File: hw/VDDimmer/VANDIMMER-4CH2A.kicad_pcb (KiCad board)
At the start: 2 copper layers, 100 x 80 mm, 96 parts, among them J1 USB-C 16P, J10 A2 V+SEL VIN/5V, J11 BTN1, J12 BTN2, J13 EXP 3V3/GND/SDA/SCL/EN/IO0, J14 UART1 3V3/GND/TX/RX, J2 VIN 9-24V, J3 CH1 V+/LED-, J4 CH2 V+/LED-, J5 CH3 V+/LED-, J6 CH4 V+/LED-, J7 ADDR1 V+/D/CLK/GND, J8 ADDR2 V+/D/CLK/GND, J9 A1 V+SEL VIN/5V, Q1 20N06, Q2 20N06, Q3 20N06, Q4 20N06, Q5 SUD50P06-15, U1 ESP32-S3-WROOM-1U-N16, U2 AP63301WU-7, U3 AMS1117-3.3, U4 74HCT125, U5 74HCT125

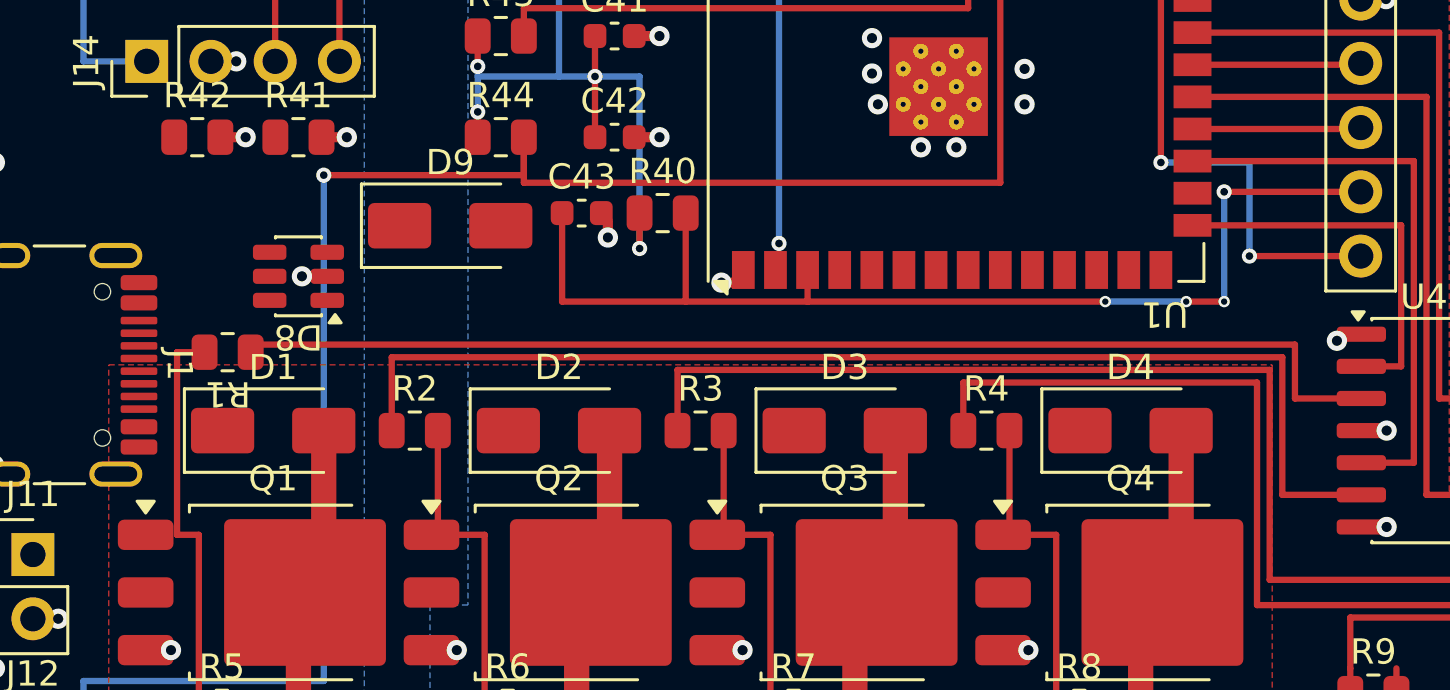
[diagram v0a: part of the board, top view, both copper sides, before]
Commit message: Re-route USB into the flipped J1; move R1 clear of the fan-out
R1 was straddling y 110.550..112.450, which after the flip is exactly where
J1's four D+/D- pads sit (111.1..112.9). With J1's pads ending at x 108.420 and
R1's courtyard starting at 109.520, the escape corridor was 1.10 mm - two lanes
for six signals.

R1 moved 2.3 mm east to (113.5, 111.5), into the 2.65 mm gap between D8's
courtyard (ends y 110.200) and D1's (starts y 112.850). Its GDRV1 pad lands at
x 113.9..114.925, still directly on GDRV1's existing y=111.2 lane, so that
connection cost nothing; only the now-stubbed western segment was trimmed.
Corridor goes 1.10 -> 3.40 mm.

GATE1 re-routed out of R1's west pad and down the back of J1 on B.Cu
(x 112.5, y 112.9..117.5, then west to 108.5) to Q1's gate, keeping it out of
the USB region entirely.

Fan-out assigned by planar ordering - source y ascending maps to turn-x
ascending, so no horizontal crosses the vertical of a pad further north:
  CC1 A5  y110.75 -> lane 108.75 -> R41.1
  DM  B7  y111.25 -> lane 109.20 -> D8.4
  DP  A6  y111.75 -> lane 109.65 -> D8.6
  DM  A7  y112.25 -> B.Cu at x110.35 (the one forced crossing)
  DP  B6  y112.75 -> lane 111.05, joins DP's run
CC2 and VBUS are boxed in by D1, so both take B.Cu: CC2 at x 108.96 down to
R42.1, VBUS south of D1 then north at x 111.2 to D8.5.

One error caught by DRC that my offline checker missed: the DM via at
(110.35, 112.25) sat 0.075 mm from DP's y=112.75 run. route.py does not
synthesise vias at layer transitions, so it only checked the tracks. Via moved
to (110.35, 112.0) and the check script now sweeps proposed vias against every
pad, track and via explicitly.

Co-Authored-By: Claude Opus 5 (1M context) <noreply@anthropic.com>
Claude-Session: https://claude.ai/code/session_01XeXr1isxVCg8kRo5Eh8BHM
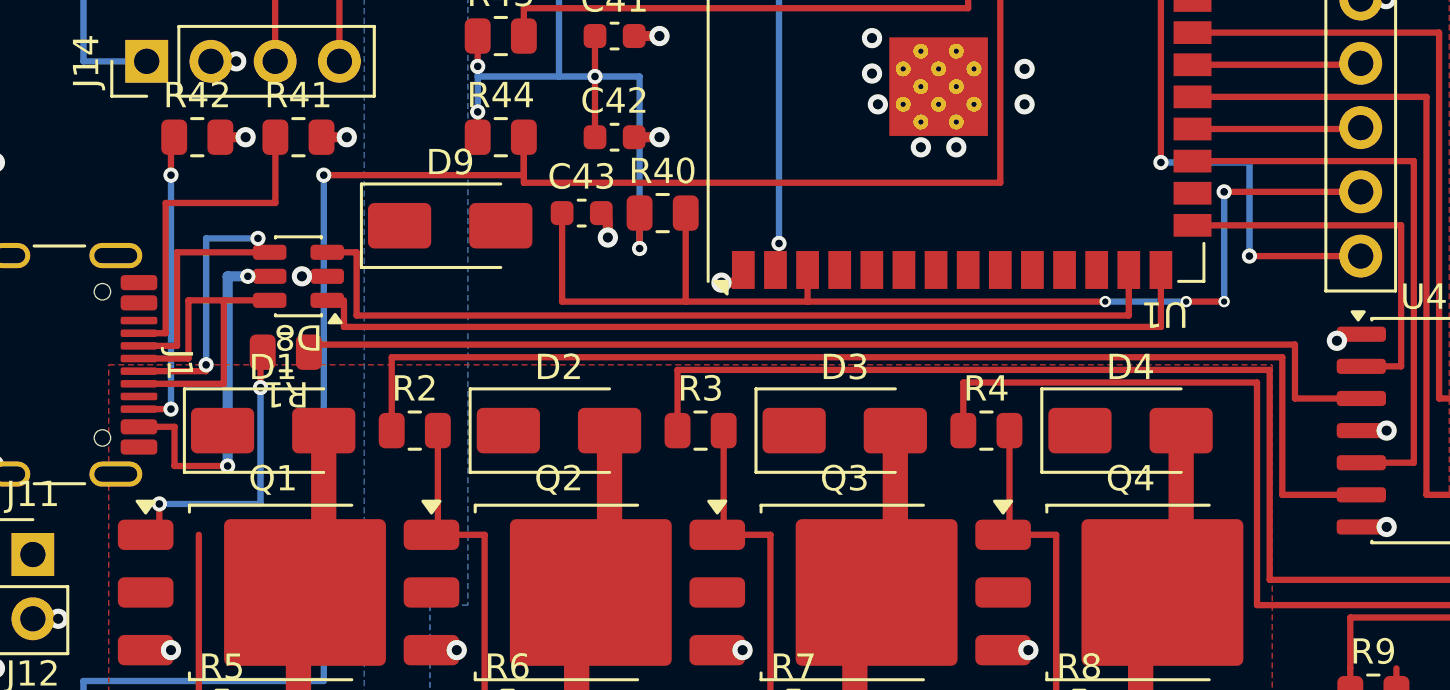
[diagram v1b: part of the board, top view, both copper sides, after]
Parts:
- moved R1 2.30 mm to (113.5, 111.5)
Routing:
- net /MCU/USB_DM: track 0.00 -> 51.7 mm, vias 0 -> 2
- net /MCU/USB_DP: track 0.00 -> 46.9 mm
- net /MCU/VBUS: track 0.00 -> 12.6 mm, vias 0 -> 2
- net /MCU/USB_CC1: track 0.00 -> 11.7 mm
- net /MCU/USB_CC2: track 0.00 -> 10.6 mm, vias 0 -> 2
- net /PWM/GDRV1: track 46.0 -> 43.8 mm
- net /PWM/GATE1: track 16.0 -> 17.4 mm, vias 0 -> 2

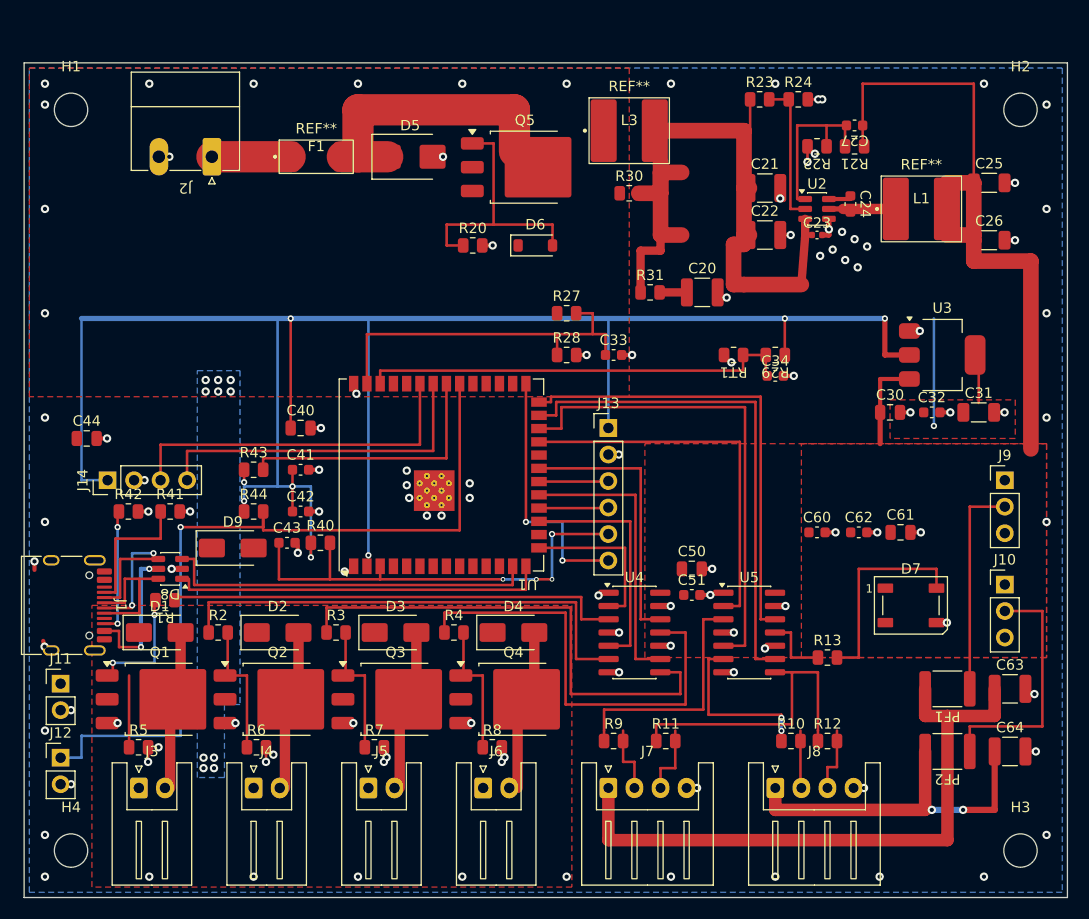
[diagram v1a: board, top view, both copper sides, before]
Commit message: Relink GATE1, brace D1's anode, re-drill sub-IPC vias, add GND return vias
- GATE1 lost the Q1-gate-to-pulldown link when the descent was re-routed; the
  1.20 mm and 6.88 mm fragments are rejoined at y=118.72.
- D1's anode was down to a single thermal spoke from the VIN_PROT pour after
  R1 moved. A 0.5 mm stub north into the pour body gives it solid copper.
- The 4 remaining 0.45/0.25 vias (all EN_MCU) gave a 0.100 mm annular ring,
  under IPC Class 2's 0.125 mm. Re-drilled to 0.45/0.20 = 0.125 exactly, which
  also still satisfies the board's own min_via_drill of 0.2. The other six of
  the original ten went out with the USB rework.
- 33 GND return vias placed, one beside each layer transition that had no
  ground via within 1.0 mm - the EMC finding kicad-happy raised and I confirmed
  (39 of 39 transitions were bare, nearest 2.47 mm, worst 8.43 mm). All 33
  positions were clearance-checked against every pad, track and via first.
  Six transitions have no room and are left bare: EN_MCU x3, VBUS x2,
  USB_DM x1.

Co-Authored-By: Claude Opus 5 (1M context) <noreply@anthropic.com>
Claude-Session: https://claude.ai/code/session_01XeXr1isxVCg8kRo5Eh8BHM
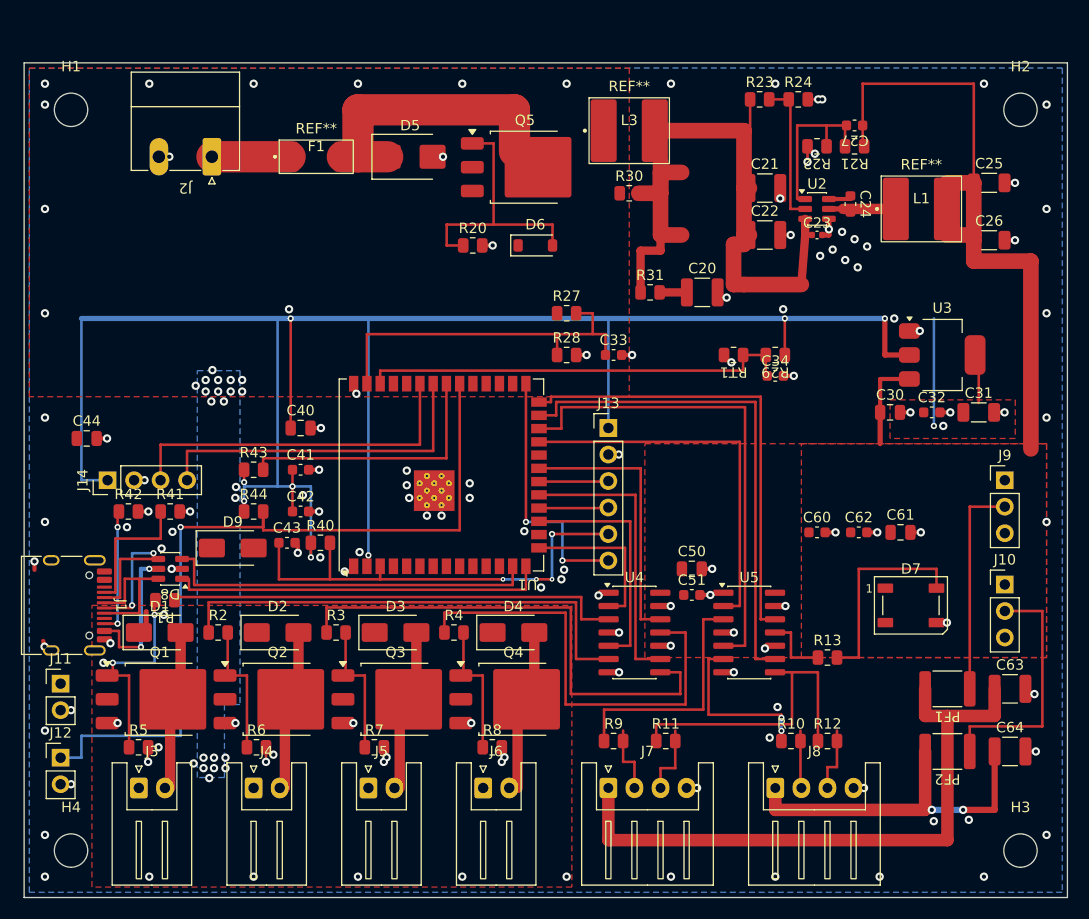
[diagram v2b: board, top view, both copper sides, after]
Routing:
- net /PWM/GATE1: track 17.4 -> 18.9 mm
- net VIN_PROT: track 0.00 -> 1.10 mm, vias 10 -> 14
- net GND: vias 116 -> 145

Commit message: Fix four dead-on-arrival defects hiding behind a clean DRC
DRC reports a split net as an unconnected item, never an error, so the board
read "0 errors" while both the gate drivers and the MCU were unpowered. All
20 unconnected items had been written off as benign; four were not.

- U4's gate drivers had no +5V. The F.Cu pour filled as two islands that did
  not touch, 448.6 mm2 carrying the main rail and 123.1 mm2 carrying only
  U4.14/C50.1/C51.1. The four-wire addressable bus runs the full height of the
  zone at 0.5 mm pitch and nothing can fill between the traces. Bridged on B.Cu
  across the bus only: +5V vias at (167.6,105.0) and (171.6,105.0), 4.0 mm of
  0.5 mm track, both vias landing inside their own island's fill.
- U1, the ESP32, had no 3V3. The via at (133.0,107.2) was exactly tangent to
  pad U1.2 -- centre-to-pad-box 0.3000 mm against a via radius of 0.3000 mm,
  zero overlap. Added a 0.5 mm F.Cu stub 0.75 mm into the pad.
- J1's north GND pad was floating; USB return had only the shell. Joined to the
  adjacent shield pad.
- Deleted a 10.3 mm orphan +3V3 B.Cu stub dangling at both ends.

Added an F.Cu GND pour at priority 0, with a bite out of the top edge at
x 172.5-186.0, y 60.5-78.5 to keep ground copper off SW and the FB divider.
75 GND vias previously touched no F.Cu copper at all, so the return vias added
in 1a1d10b were inert. via_dangling 81 -> 9, GND groups 2 -> 1, warnings
244 -> 170, unconnected 18 -> 15. Zone set to solid pad connection to clear
six starved_thermal errors.

Tooling: measure.py did not run as committed (missing import, two wrong call
signatures, a zone parser matching spaces against a tab-indented file). New
connect.py groups each net's copper into connected components and is what found
all four defects; its first version treated a touching via and pad as connected,
which is precisely the U1.2 case, so it now requires real overlap and reports
contacts thinner than 50 um. Also polyidx.py, emc.py, retvia.py.

Co-Authored-By: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
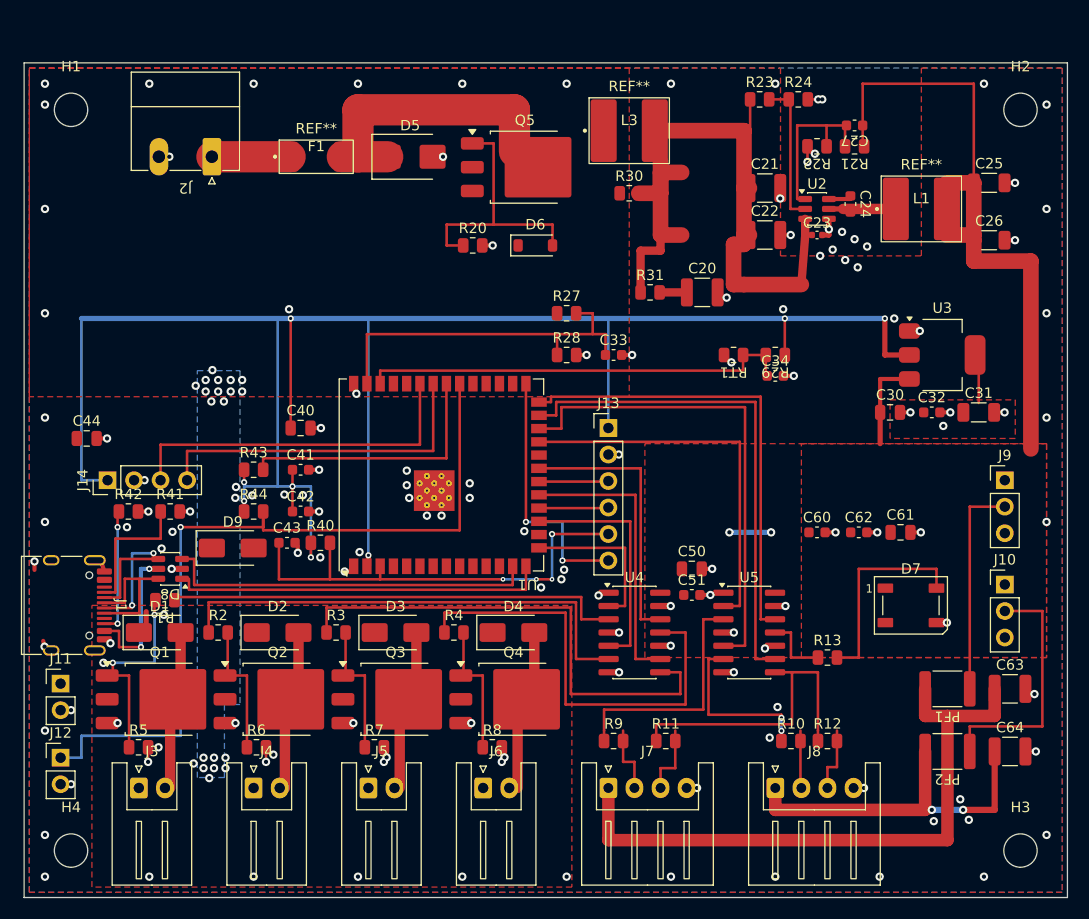
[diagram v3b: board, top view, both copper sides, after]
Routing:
- net +3V3: track 195.5 -> 186.3 mm, vias 9 -> 8
- net +5V: track 69.1 -> 73.1 mm, vias 0 -> 2
- net GND: track 27.3 -> 28.4 mm, vias 145 -> 148
- added copper zone on F.Cu, net GND
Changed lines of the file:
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@@
 		(net "+5V")
 	)
+	(via
+		(at 167.6 105)
+		(size 0.8)
+		(drill 0.4)
+		(layers "F.Cu" "B.Cu")
+		(net "+5V")
+	)
+	(via
+		(at 171.6 105)
+		(size 0.8)
+		(drill 0.4)
+		(layers "F.Cu" "B.Cu")
+		(net "+5V")
+	)
+	(segment
+		(start 167.6 105)
+		(end 171.6 105)
+		(width 0.5)
+		(layer "B.Cu")
+		(net "+5V")
+	)
 	(segment
 		(start 123.186 125.6)
@@
 	)
 	(segment
+		(start 107.695 108.75)
+		(end 107.35 107.68)
+		(width 0.4)
+		(layer "F.Cu")
+		(net "GND")
+	)
+	(segment
 		(start 175.113 63.5)
 		(end 176.5 63.5)
@@
 	)
 	(via
+		(at 189.728 130.586)
+		(size 0.8)
+		(drill 0.4)
+		(layers "F.Cu" "B.Cu")
+		(net "GND")
+	)
+	(via
 		(at 125.394 83.614)
 		(size 0.8)
@@
 	)
 	(via
+		(at 124.947 101.378)
+		(size 0.8)
+		(drill 0.4)
+		(layers "F.Cu" "B.Cu")
+		(net "GND")
+	)
+	(via
 		(at 116.447 90.95)
 		(size 0.8)
@@
 	)
 	(via
+		(at 121.866 101.455)
+		(size 0.8)
+		(drill 0.4)
+		(layers "F.Cu" "B.Cu")
+		(net "GND")
+	)
+	(via
 		(at 165.775 111)
 		(size 0.8)
@@
 	)
 	(segment
+		(start 133 107.2)
+		(end 133 108.25)
+		(width 0.5)
+		(layer "F.Cu")
+		(net "+3V3")
+	)
+	(segment
 		(start 127.488 107.4)
 		(end 127.488 106.4)
@@
 	)
 	(via
-		(at 187.2 94.8)
-		(size 0.6)
-		(drill 0.3)
-		(layers "F.Cu" "B.Cu")
-		(net "+3V3")
-	)
-	(via
 		(at 182.5 84.5)
 		(size 0.6)
@@
 	)
 	(segment
-		(start 187.2 84.5)
-		(end 187.2 94.8)
-		(width 0.25)
-		(layer "B.Cu")
-		(net "+3V3")
-	)
-	(segment
 		(start 124.3 100.6)
 		(end 127.488 100.6)
@@
 			)
 		)
+	)
+	(zone
+		(net "GND")
+		(layer "F.Cu")
+		(hatch edge 0.508)
+		(connect_pads yes
+			(clearance 0.2)
+		)
+		(min_thickness 0.25)
+		(fill yes
+			(thermal_gap 0.5)
+			(thermal_bridge_width 0.5)
+			(island_removal_mode 0)
+		)
+		(polygon
+			(pts
+				(xy 100.5 60.5) (xy 172.5 60.5) (xy 172.5 78.5) (xy 186 78.5) (xy 186 60.5) (xy 199.5 60.5) (xy 199.5 139.5)
+				(xy 100.5 139.5)
+			)
+		)

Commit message: Fix six drill defects, fit the I2C pull-ups, add the board ID
Drill defects
-------------
hole_to_hole and holes_co_located are downgraded to warning in .kicad_pro, so
the board reported "DRC 0 errors" while carrying five hole_to_hole and one
holes_co_located -- two of them with physically overlapping drills. Same shape
of trap as the split-net lesson already in HANDOFF.

Five vias deleted, each proven non-load-bearing first by checking which track
endpoints actually land on it. In every overlapping pair only one via carried a
track; the other was a bare stitching via with its twin 0.1-0.5 mm away.
d85c5d26 was redundant by construction -- 1 mm from J2's PTH GND pad, which
already ties both layers. afb88017 was an exact duplicate of a14092cd.
Afterwards GND is still one connected group, the split-net count is unchanged
at 12, and via count went 192 -> 187.

I2C pull-ups (R45, R46)
-----------------------
4.7k 0805, C17673, per the 2026-08-29 decision. Verified against the exported
netlist rather than the tools' return values, because the pins are tied with a
plain +3V3 net label -- the convention J13's own supply pin uses on this sheet.
Had that not merged with the power net the pull-ups would have pulled to
nothing, which is the silent failure the decision existed to prevent.

  +3V3          15 nodes  ... J13.1 R43.1 R44.1 R45.1 R46.1 U1.2 U3.2
  /MCU/I2C_SDA   3 nodes  J13.3  R45.2  U1.20
  /MCU/I2C_SCL   3 nodes  J13.4  R46.2  U1.18

The taps run on B.Cu because ADDR1_DIN crosses the whole board on F.Cu at
y=96.33, x 149.35-168.60, walling +3V3 (which reaches J13.1 at y=95) off from
the I2C lines at y=100.14 and 102.67. There is no F.Cu-only path; going round
its east end costs ~30 mm and still needs via hops over the GATE_IN verticals.
B.Cu there is bare GND pour and J13's pads 1/3/4 are through-hole, so they are
reachable from below with no via at that end.

Both parts are rotated 180 deg. They arrive with pad 1 (+3V3) west, which would
force the SDA return to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
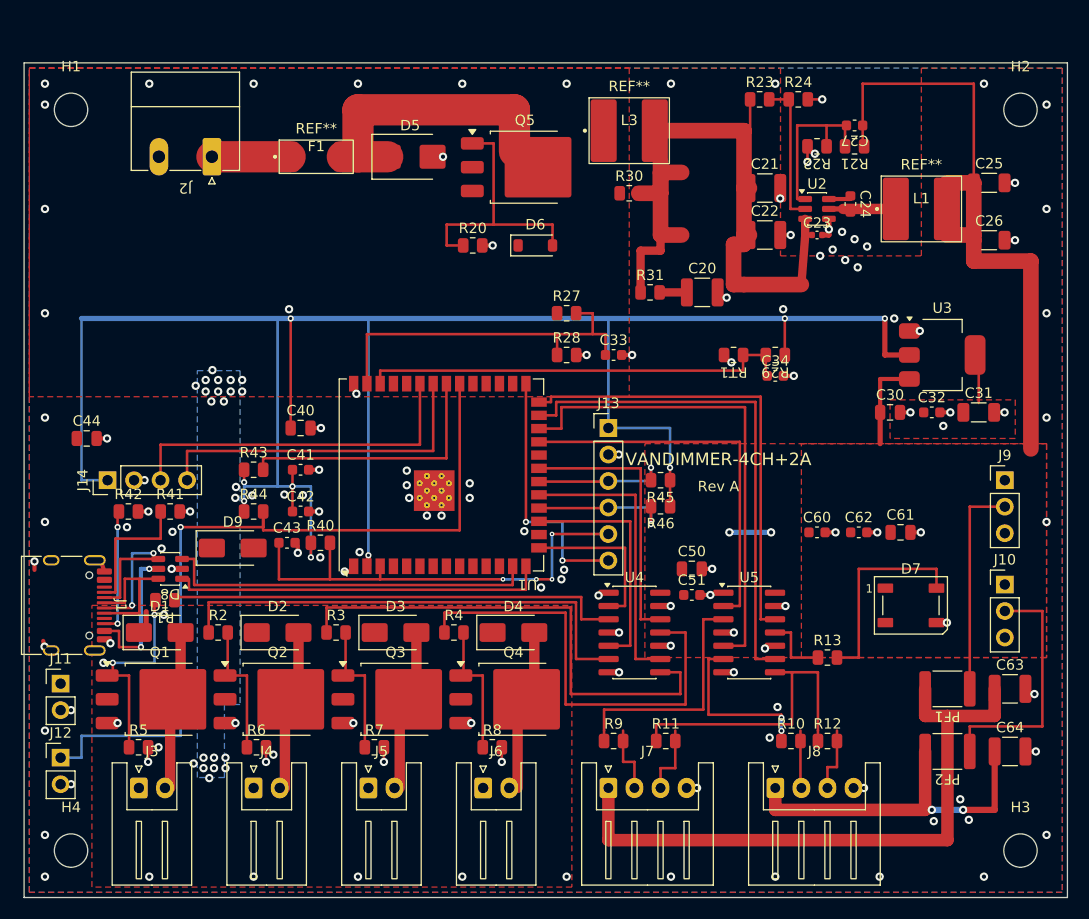
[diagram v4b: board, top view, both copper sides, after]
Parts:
- added R45: 4.7k, Resistor_SMD:R_0805_2012Metric, F.Cu at (161.0, 100.0)
- added R46: 4.7k, Resistor_SMD:R_0805_2012Metric, F.Cu at (161.0, 102.5)
- F1: value 10A 250V -> 8A 250V
- J2: value VIN 9-24V -> VIN 12V
- R11, R12: value 47R DNP -> 47R
- U3: value AMS1117-3.3 -> BL1117-33CX
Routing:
- net +3V3: track 186.3 -> 199.7 mm, vias 8 -> 9
- net /MCU/I2C_SCL: track 6.65 -> 14.0 mm, vias 0 -> 1
- net /MCU/I2C_SDA: track 6.65 -> 13.2 mm, vias 0 -> 1
- net GND: vias 148 -> 144
- net /MCU/EN_MCU: vias 5 -> 4
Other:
- board text added: "Rev A"
- board text added: "VANDIMMER-4CH+2A"
